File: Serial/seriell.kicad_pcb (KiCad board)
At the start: 2 copper layers, 145 x 68 mm, 29 parts, among them J1 Conn_01x10_Pin, J10 Conn_01x06, J11 Conn_01x06, J12 TTL, J13 Conn_01x10_Pin, J14 Conn_01x10_Pin, J15 Conn_01x10_Pin, J16 Conn_01x10_Pin, J17 Conn_01x10_Pin, J18 Conn_01x10_Pin, J19 Bluetooth, J2 Conn_01x10_Pin, J20 Conn_01x04, J3 Conn_01x10_Pin, J30 Flash, J4 Conn_01x10_Pin, J5 Conn_01x10_Pin, J6 Conn_01x10_Pin, J7 Conn_02x04_Counter_Clockwise, J8 BT

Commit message: flash
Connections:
- J1 pad 10: Net-(J1-Pin_10) -> GND
- J10 pad 2: Net-(J1-Pin_10) -> GND
- J11 pad 6: Net-(J1-Pin_10) -> GND
- J12 pad 1: Net-(J1-Pin_10) -> GND
- J13 pad 10: Net-(J1-Pin_10) -> GND
- J20 pad 1: Net-(J1-Pin_10) -> GND
- J8 pad 3: Net-(J1-Pin_10) -> GND
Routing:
- net Net-(J1-Pin_10): track 251.3 -> 0.00 mm, vias 2 -> 0
- net GND: track 59.3 -> 310.6 mm, vias 0 -> 2
- added copper zone on B.Cu, net GND
- added copper zone on F.Cu, net GND

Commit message: serial redesign
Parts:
- removed J19: Bluetooth, Connector_PinHeader_2.54mm:PinHeader_1x02_P2.54mm_Vertical
- removed J30: Flash, Connector_PinHeader_2.54mm:PinHeader_2x03_P2.54mm_Vertical
- added JP1: Bluetooth, Jumper:SolderJumper-2_P1.3mm_Open_Pad1.0x1.5mm, B.Cu at (116.3, 115.5)
- added JP2: RX, Jumper:SolderJumper-2_P1.3mm_Open_Pad1.0x1.5mm, B.Cu at (175.0, 128.5)
- added JP3: TX, Jumper:SolderJumper-2_P1.3mm_Open_Pad1.0x1.5mm, B.Cu at (176.5, 126.0)
- J20: value Conn_01x04 -> Auslesen
- moved REF** 53.6 mm to (120.0, 95.5)
- moved R1 31.4 mm to (198.0, 130.4)
- moved R2 23.1 mm to (191.0, 130.4)
- moved R3 16.8 mm to (184.5, 130.4)
- moved J20 6.82 mm to (207.5, 130.0)
- moved J7 5.67 mm to (211.5, 90.8)
- moved D1 3.08 mm to (184.5, 136.0)
- moved D3 3.07 mm to (198.0, 136.0)
- moved D2 3.06 mm to (191.1, 136.0)
- moved A1 2.95 mm to (181.0, 119.5)
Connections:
- net Net-(J1-Pin_1) renamed +5V
- net Net-(J10-Pin_3) renamed TX
- A1 pad 1: unconnected-(A1-D1/TX-Pad1) -> Net-(A1-D1/TX)
- A1 pad 2: unconnected-(A1-D0/RX-Pad2) -> Net-(A1-D0/RX)
- J10 pad 1: Net-(J10-Pin_1) -> unconnected-(J10-Pin_1-Pad1)
- J10 pad 4: Net-(J10-Pin_4) -> RX
- J10 pad 5: Net-(J10-Pin_1) -> unconnected-(J10-Pin_5-Pad5)
- J11 pad 2: Net-(J10-Pin_4) -> RX
- J12 pad 2: Net-(J10-Pin_4) -> RX
- J14 pad 8: Net-(J10-Pin_4) -> RX
- J2 pad 8: Net-(J10-Pin_4) -> RX
- J20 pad 2: Net-(J10-Pin_4) -> RX
- J8 pad 1: unconnected-(J8-Pin_1-Pad1) -> RX
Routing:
- net Net-(J10-Pin_4): track 226.5 -> 0.00 mm
- net GND: track 310.6 -> 103.8 mm, vias 2 -> 54
- net RX: track 0.00 -> 172.4 mm
- net TX: track 292.5 -> 168.0 mm, vias 0 -> 2
- net Net-(D3-K): track 49.7 -> 4.68 mm
- net Net-(D2-K): track 37.9 -> 4.73 mm
- net Net-(A1-+5V): track 56.1 -> 81.6 mm
- net Net-(D1-K): track 27.0 -> 4.68 mm
- net unconnected-(J8-Pin_1-Pad1): track 20.4 -> 0.00 mm
- net Net-(A1-D0/RX): track 0.00 -> 18.6 mm
- net Net-(J10-Pin_1): track 14.1 -> 0.00 mm
- net +5V: track 167.9 -> 153.9 mm, vias 2 -> 1
- net Net-(A1-D1/TX): track 0.00 -> 11.9 mm
- net Net-(J8-Pin_4): track 25.4 -> 15.1 mm
- net Net-(A1-3V3): track 63.4 -> 54.7 mm
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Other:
- board size 145 x 68 mm -> 136 x 62 mm
- board text added: "Arduino <->DB"
- board text added: "offen=aus"
- board text added: "zu=an"
- board text removed: "Auslesen"
- board text removed: "closed=on"
- board text removed: "open=off"

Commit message: wemos
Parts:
- added U1: WeMos_D1_mini, Module:WEMOS_D1_mini_light, F.Cu at (110.1, 80.7)
- D2: value Error -> Fehler
- D3: value Power -> Bereit
- moved JP2 51.3 mm to (141.5, 89.7), turned to 90 degrees
- moved JP3 49.9 mm to (144.0, 88.2), turned to 90 degrees
- moved REF** 37.4 mm to (110.0, 131.5)
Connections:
- net Net-(A1-+5V) renamed +5VA
- net Net-(A1-3V3) renamed +3.3V
- net Net-(A1-D10) renamed /CS
- net Net-(A1-D11) renamed /MOSI
- net Net-(A1-D12) renamed /MISO
- net Net-(A1-D13) renamed /SCK
- A1 pad 1: Net-(A1-D1/TX) -> unconnected-(A1-D1/TX-Pad1)
- A1 pad 2: Net-(A1-D0/RX) -> unconnected-(A1-D0/RX-Pad2)
- JP2 pad 2: Net-(A1-D0/RX) -> Net-(JP2-B)
- JP3 pad 2: Net-(A1-D1/TX) -> Net-(JP3-B)
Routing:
- net Net-(A1-D9): track 59.5 -> 198.1 mm
- net Net-(A1-D8): track 51.3 -> 150.8 mm
- net Net-(A1-D7): track 46.7 -> 134.7 mm
- net /MISO: track 32.3 -> 106.9 mm
- net /CS: track 31.2 -> 105.9 mm
- net /MOSI: track 28.9 -> 103.5 mm
- net GND: track 103.8 -> 29.4 mm, vias 54 -> 61
- net +3.3V: track 54.7 -> 127.6 mm, vias 0 -> 1
- net /SCK: track 45.5 -> 103.0 mm
- net +5VA: track 81.6 -> 128.8 mm, vias 0 -> 1
- net Net-(A1-D0/RX): track 18.6 -> 0.00 mm
- net Net-(JP3-B): track 0.00 -> 15.0 mm
- net Net-(A1-D1/TX): track 11.9 -> 0.00 mm
- net Net-(JP2-B): track 0.00 -> 10.9 mm
- net TX: track 168.0 -> 158.7 mm
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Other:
- board text added: "Wemos <->DB"
- board text removed: "Arduino <->DB"

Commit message: esp
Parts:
- removed A1: Arduino_Nano_v3.x, Module:Arduino_Nano
- removed J10, J11: Conn_01x06, Connector_PinHeader_2.54mm:PinHeader_1x06_P2.54mm_Vertical
- removed J12: TTL, Connector_PinHeader_2.54mm:PinHeader_1x06_P2.54mm_Vertical
- removed J13, J14, J15, J16, J17, J18, J5, J6: Conn_01x10_Pin, Connector_PinSocket_2.54mm:PinSocket_1x10_P2.54mm_Vertical
- removed J20: Auslesen, Connector_PinHeader_2.54mm:PinHeader_1x04_P2.54mm_Vertical
- removed J8: BT, Connector_PinHeader_2.54mm:PinHeader_1x04_P2.54mm_Vertical
- removed JP1: Bluetooth, Jumper:SolderJumper-2_P1.3mm_Open_Pad1.0x1.5mm
- removed JP2: RX, Jumper:SolderJumper-2_P1.3mm_Open_Pad1.0x1.5mm
- removed JP3: TX, Jumper:SolderJumper-2_P1.3mm_Open_Pad1.0x1.5mm
- removed REF**: OSHW-Logo2_9.8x8mm_SilkScreen, Symbol:OSHW-Logo2_9.8x8mm_SilkScreen
- removed REF**: WEEE-Logo_8.4x12mm_SilkScreen, Symbol:WEEE-Logo_8.4x12mm_SilkScreen
- added C1: 10uF, Capacitor_SMD:C_0603_1608Metric, F.Cu at (129.5, 112.5)
- added C2: 10uF, Capacitor_SMD:C_0603_1608Metric, F.Cu at (129.5, 117.6)
- added D4: D, Diode_SMD:D_SOD-123, F.Cu at (109.2, 96.5)
- added P1: USB_C_Plug_USB2.0, Connector_USB:USB_C_Receptacle_G-Switch_GT-USB-7010ASV, F.Cu at (179.6, 94.4)
- added U2: AMS1117-3.3, Package_TO_SOT_SMD:SOT-223-3_TabPin2, F.Cu at (136.6, 114.3)
- D1, D2, D3: footprint LED_THT:LED_D5.0mm -> LED_SMD:LED_0603_1608Metric
- J1, J3: value Conn_01x10_Pin -> Datenbank; footprint Connector_PinSocket_2.54mm:PinSocket_1x10_P2.54mm_Vertical -> Connector_DIN:DIN41612_C3_3x10_Female_Vertical_THT
- J2, J4: value Conn_01x10_Pin -> Steuereinheit; footprint Connector_PinSocket_2.54mm:PinSocket_1x10_P2.54mm_Vertical -> Connector_DIN:DIN41612_R3_3x10_Male_Vertical_THT; moved to B.Cu
- J7: footprint Connector_PinHeader_2.54mm:PinHeader_2x04_P2.54mm_Vertical -> Connector_IDC:IDC-Header_2x04_P2.54mm_Vertical
- R1, R2, R3: footprint Resistor_SMD:R_0805_2012Metric -> LED_SMD:LED_0603_1608Metric
- U1: value WeMos_D1_mini -> ESP32-C3-WROOM-02; footprint Module:WEMOS_D1_mini_light -> RF_Module:ESP32-C3-WROOM-02
- moved J3 108.2 mm to (199.0, 99.7)
- moved J7 84.7 mm to (127.0, 96.5), turned to -90 degrees
- moved U1 44.3 mm to (150.6, 98.6)
- moved J4 26.0 mm to (211.1, 122.6)
- moved J2 24.9 mm to (98.0, 122.6)
- moved R3 16.9 mm to (167.6, 128.8), turned to -90 degrees
- moved R2 15.8 mm to (175.3, 128.8), turned to -90 degrees
- moved R1 15.2 mm to (182.9, 128.8), turned to -90 degrees
- moved D1 14.1 mm to (171.9, 129.5)
- moved D2 13.3 mm to (179.6, 129.5)
- moved D3 12.6 mm to (187.2, 129.5)
- moved J1 0.26 mm to (86.0, 99.7)
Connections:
- D1 pad 2: Net-(A1-D7) -> Net-(D1-A)
- D2 pad 2: Net-(A1-D8) -> Net-(D2-A)
- D3 pad 2: Net-(A1-D9) -> Net-(D3-A)
- U1 pad 1: unconnected-(U1-~{RST}-Pad1) -> +3.3V
- U1 pad 10: GND -> /SCK
- U1 pad 11: Net-(A1-D7) -> RX
- U1 pad 12: Net-(A1-D8) -> TX
- U1 pad 13: unconnected-(U1-SDA/D2-Pad13) -> Net-(P1-D-)
- U1 pad 14: unconnected-(U1-SCL/D1-Pad14) -> Net-(P1-D+)
- U1 pad 15: Net-(JP2-B) -> Net-(D3-A)
- U1 pad 16: Net-(JP3-B) -> Net-(D2-A)
- U1 pad 3: Net-(A1-D9) -> unconnected-(U1-IO4-Pad3)
- U1 pad 4: /SCK -> unconnected-(U1-IO5-Pad4)
- U1 pad 5: /MISO -> unconnected-(U1-IO6-Pad5)
- U1 pad 6: /MOSI -> /CS
- U1 pad 7: /CS -> /MOSI
- U1 pad 8: +3.3V -> /MISO
- U1 pad 9: +5VA -> GND
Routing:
- net Net-(A1-D9): track 198.1 -> 0.00 mm, vias 1 -> 0
- net Net-(A1-D8): track 150.8 -> 0.00 mm, vias 1 -> 0
- net Net-(A1-D7): track 134.7 -> 0.00 mm, vias 1 -> 0
- net /MOSI: track 103.5 -> 19.1 mm
- net /CS: track 105.9 -> 21.6 mm
- net RX: track 171.1 -> 89.0 mm, vias 0 -> 1
- net /MISO: track 106.9 -> 26.7 mm, vias 0 -> 1
- net TX: track 158.7 -> 88.4 mm, vias 2 -> 0
- net +3.3V: track 127.6 -> 61.7 mm, vias 1 -> 0
- net /SCK: track 103.0 -> 40.8 mm, vias 0 -> 1
- net +5VA: track 128.8 -> 69.6 mm
- net Net-(D3-A): track 0.00 -> 55.1 mm, vias 0 -> 2
- net Net-(D2-A): track 0.00 -> 52.4 mm, vias 0 -> 2
- net Net-(D1-A): track 0.00 -> 48.3 mm, vias 0 -> 2
- net GND: track 29.4 -> 76.6 mm, vias 61 -> 11
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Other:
- board size 136 x 62 mm -> 134.6 x 40.6 mm
- board text removed: "5V"
- board text removed: "DB"
- board text removed: "GND"
- board text removed: "MISO"
- board text removed: "MOSI"
- board text removed: "PD4"
- board text removed: "RST"
- board text removed: "RX"
- board text removed: "SCK"
- board text removed: "ST"
- board text removed: "TX"
- board text removed: "VCC"
- board text removed: "Wemos <->DB"
- board text removed: "offen=aus"
- board text removed: "zu=an"

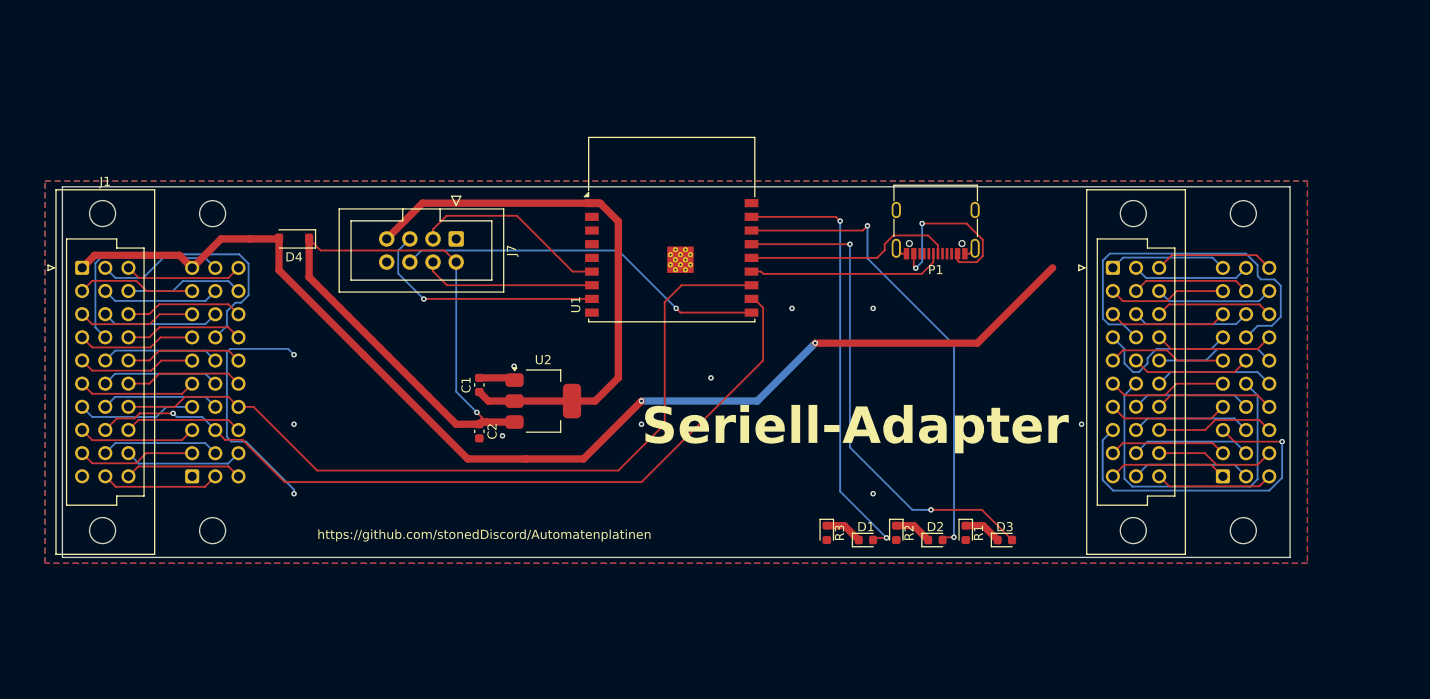
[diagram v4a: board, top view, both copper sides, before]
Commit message: usbasp stecker
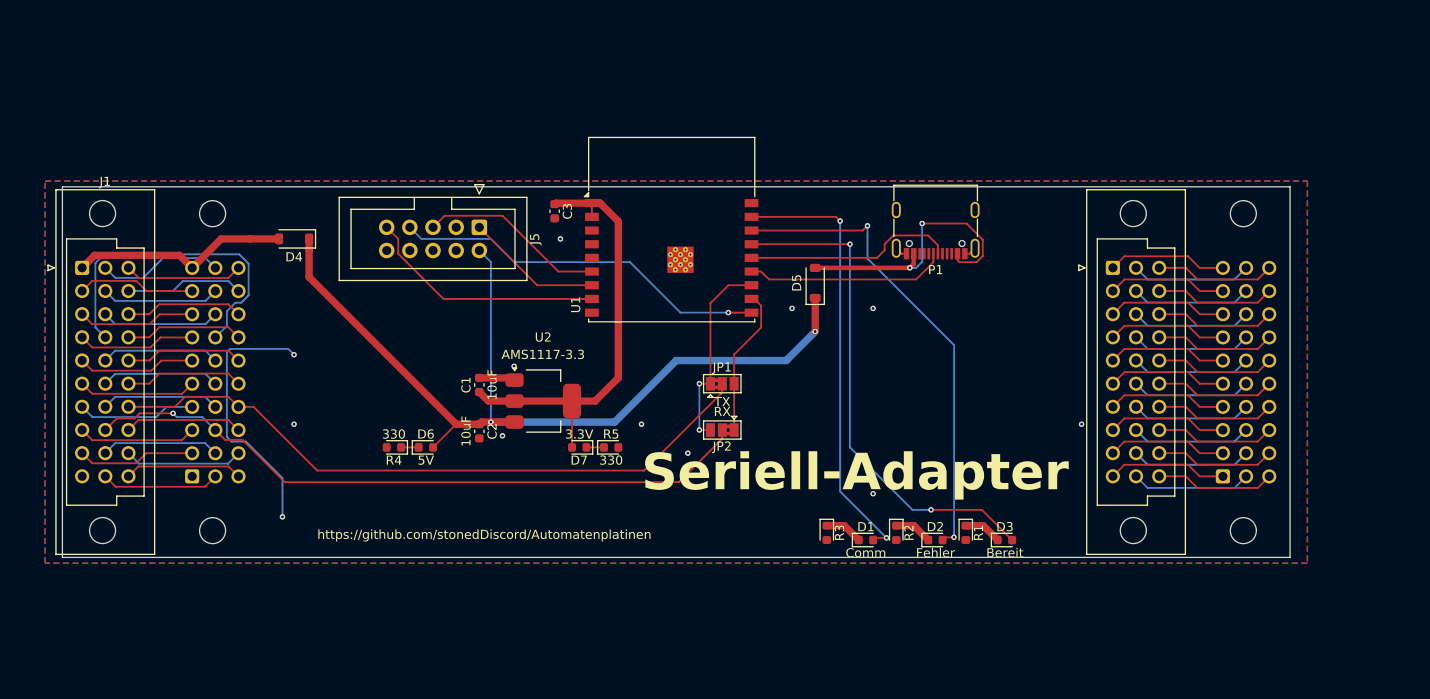
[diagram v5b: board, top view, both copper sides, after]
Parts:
- removed J7: Conn_02x04_Counter_Clockwise, Connector_IDC:IDC-Header_2x04_P2.54mm_Vertical
- added C3: 10uF, Capacitor_SMD:C_0603_1608Metric, F.Cu at (137.8, 93.5)
- added D5: D, Diode_SMD:D_SOD-123, F.Cu at (166.4, 101.3)
- added D6: 5V, LED_SMD:LED_0603_1608Metric, F.Cu at (123.7, 119.4)
- added D7: 3.3V, LED_SMD:LED_0603_1608Metric, F.Cu at (140.5, 119.4)
- added J5: Conn_02x05_Odd_Even, Connector_IDC:IDC-Header_2x05_P2.54mm_Vertical, F.Cu at (129.5, 95.2)
- added JP1: TX, Jumper:SolderJumper-3_P1.3mm_Bridged2Bar12_Pad1.0x1.5mm, F.Cu at (156.2, 112.4)
- added JP2: RX, Jumper:SolderJumper-3_P1.3mm_Bridged2Bar12_Pad1.0x1.5mm, F.Cu at (156.2, 117.5)
- added R4: 330, LED_SMD:LED_0603_1608Metric, F.Cu at (120.2, 119.4)
- added R5: 330, LED_SMD:LED_0603_1608Metric, F.Cu at (144.0, 119.4)
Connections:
- J3 pad a10: GND -> Net-(J3A-Pin_a10)
- J3 pad a4: GND -> Net-(J3A-Pin_a4)
- J4 pad a1: GND -> Net-(J3A-Pin_a10)
- J4 pad a7: GND -> Net-(J3A-Pin_a4)
- U1 pad 11: RX -> Net-(JP1-B)
- U1 pad 12: TX -> Net-(JP1-A)
- U1 pad 2: unconnected-(U1-EN-Pad2) -> +3.3V
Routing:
- net +5V: track 129.6 -> 24.0 mm, vias 2 -> 0
- net +5VA: track 69.6 -> 99.8 mm, vias 1 -> 2
- net Net-(J3B-Pin_b4): track 41.0 -> 13.1 mm
- net GND: track 76.6 -> 49.0 mm, vias 11 -> 12
- net Net-(J3A-Pin_a8): track 37.7 -> 13.1 mm, vias 1 -> 0
- net Net-(J3B-Pin_b6): track 37.2 -> 13.1 mm
- net Net-(JP1-A): track 0.00 -> 21.9 mm, vias 0 -> 2
- net Net-(JP1-B): track 0.00 -> 16.2 mm
- net TX: track 88.4 -> 73.4 mm
- net RX: track 89.0 -> 74.5 mm
- net Net-(J3A-Pin_a10): track 0.00 -> 13.1 mm
- net Net-(J3A-Pin_a4): track 0.00 -> 13.1 mm
- net +3.3V: track 61.7 -> 49.2 mm
- net VBUS: track 19.9 -> 31.2 mm
- net /MOSI: track 19.1 -> 15.0 mm
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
